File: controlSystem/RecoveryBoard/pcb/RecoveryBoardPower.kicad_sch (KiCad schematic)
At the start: 65 parts, among them J1 Conn_01x06, J10 Conn_01x02, J2 Thermistor, J3 Conn_01x04, J8 Conn_01x06, Q1 SI7465DP-T1-E3, U2 MP26123DR-LF-Z, U3 TPS63070

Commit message: Added rocket ready connector to ERS board
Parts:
- C10: value 100n -> 2.2n
- D4: value 1N4007 -> SS210A
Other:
- note removed: "ADD FLIGHT READY OR SIMiLAR PLUG"
- note removed: "ADD SEPARATE CONNECTOR FOR UMB INPUT ON INTERFACE BOARD?"
- note removed: "Check compv values"
- note removed: "Check values"
- note removed: "Swap for SS210A?"
- note removed: "Todo: Fix land pattern for footprint"
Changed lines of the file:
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@@
-    (effects (font (size 2.032 2.032)) (justify left bottom))
-  )
-  (text "ADD SEPARATE CONNECTOR FOR UMB INPUT ON INTERFACE BOARD?"
-    (at 73.66 134.62 0)
     (effects (font (size 2.032 2.032)) (justify left bottom))
   )
@@
     (effects (font (size 2.54 2.54)) (justify left bottom))
   )
-  (text "Swap for SS210A?" (at 220.98 129.54 0)
-    (effects (font (size 3.048 3.048)) (justify left bottom))
-  )
   (text "3S1P LiPo Battery" (at 281.94 132.08 0)
     (effects (font (size 1.27 1.27)) (justify left bottom))
@@
   )
   (text "Normally on\nShort ARM-IN with ARM-OUT to turn off" (at 266.7 48.26 0)
-    (effects (font (size 1.27 1.27)) (justify left bottom))
-  )
-  (text "Check compv values" (at 223.52 172.72 0)
     (effects (font (size 1.27 1.27)) (justify left bottom))
   )
@@
     (at 78.74 83.82 0)
     (effects (font (size 1.27 1.27)) (justify left bottom))
-  )
-  (text "Todo: Fix land pattern for footprint" (at 209.55 239.395 0)
-    (effects (font (size 1.27 1.27)) (justify left bottom))
-  )
-  (text "Check values" (at 220.98 228.6 0)
-    (effects (font (size 1.27 1.27)) (justify left bottom))
-  )
-  (text "ADD FLIGHT READY OR SIMiLAR PLUG" (at 73.66 139.7 0)
-    (effects (font (size 2.032 2.032)) (justify left bottom))
   )
   (text "LiPo Battery Charger" (at 208.28 101.6 0)
@@
       (effects (font (size 1.27 1.27)) (justify left))
     )
-    (property "Value" "100n" (id 1) (at 228.6 158.7562 0)
+    (property "Value" "2.2n" (id 1) (at 228.6 158.7562 0)
       (effects (font (size 1.27 1.27)) (justify left))
     )
@@
       (effects (font (size 1.27 1.27)) (justify left))
     )
-    (property "Value" "1N4007" (id 1) (at 228.6 125.4759 90)
-      (effects (font (size 1.27 1.27)) (justify left))
-    )
+    (property "Value" "SS210A" (id 1) (at 228.6 125.4759 90)
+      (effects (font (size 1.27 1.27)) (justify left))
+    )

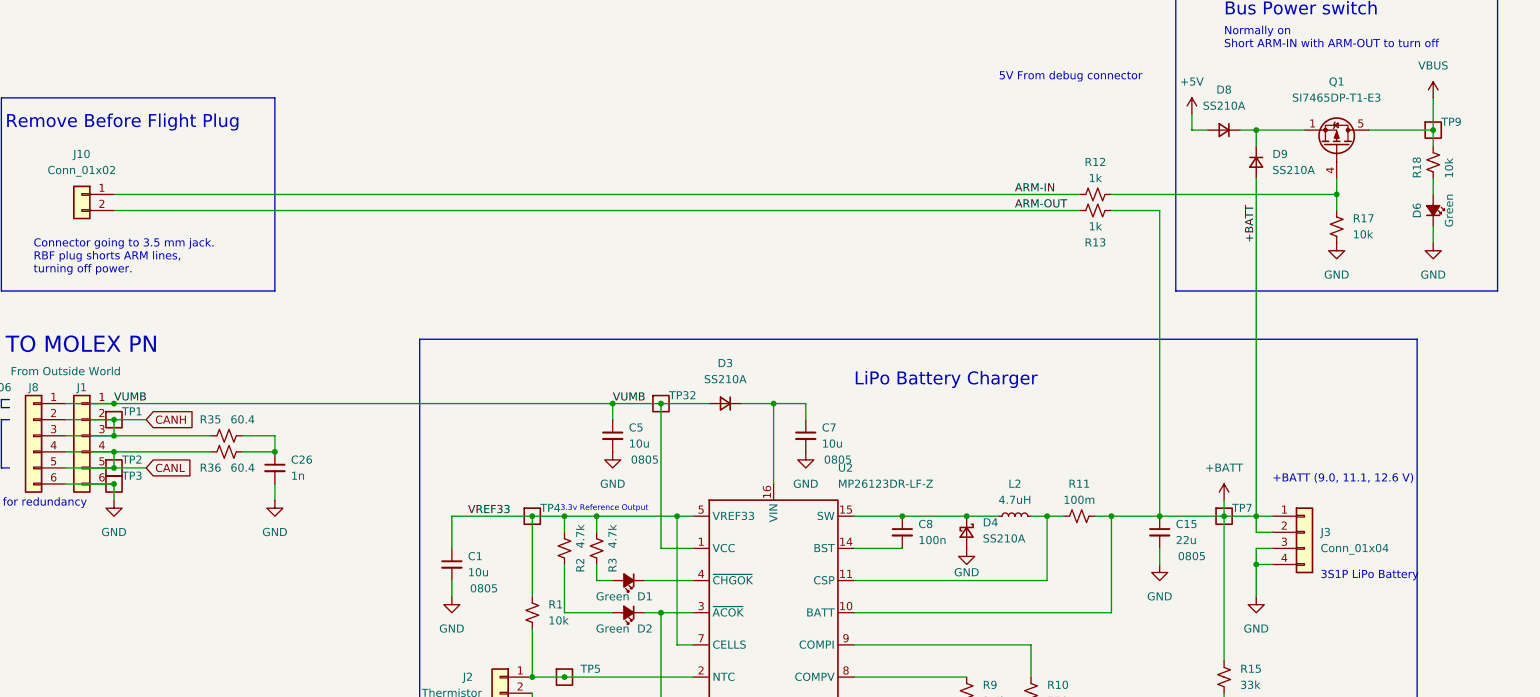
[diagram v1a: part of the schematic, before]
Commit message: Design review changes and cleaned up board layout.
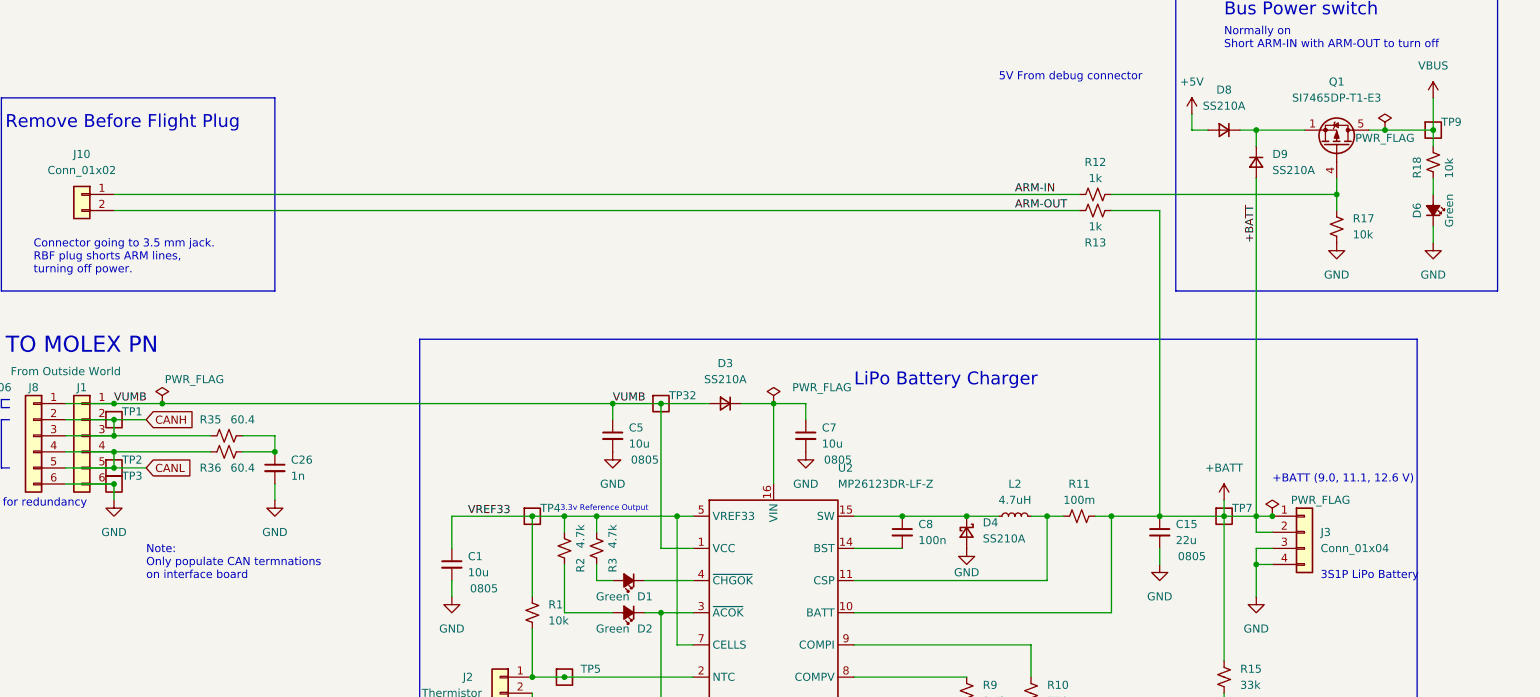
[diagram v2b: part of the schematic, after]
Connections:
- net +3.3V: now also U3.TIE2 (VOUT)
- net VBUS: now also U3.TIE1 (VIN)
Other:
- note added: "Note: Only populate CAN termnations on interface board"
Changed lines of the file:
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@@
   (junction (at 256.54 121.92) (diameter 0) (color 0 0 0 0)
   )
+  (junction (at 292.1 60.96) (diameter 0) (color 0 0 0 0)
+  )
   (junction (at 299.72 60.96) (diameter 0) (color 0 0 0 0)
   )
@@
   (junction (at 91.44 111.76) (diameter 0) (color 0 0 0 0)
   )
+  (junction (at 99.06 104.14) (diameter 0) (color 0 0 0 0)
+  )
   (junction (at 167.64 121.92) (diameter 0) (color 0 0 0 0)
   )
@@
   )
   (junction (at 271.78 60.96) (diameter 0) (color 0 0 0 0)
+  )
+  (junction (at 274.32 121.92) (diameter 0) (color 0 0 0 0)
   )
   (junction (at 91.44 114.3) (diameter 0) (color 0 0 0 0)
@@
     (stroke (width 0) (type default) (color 0 0 0 0))
   )
-  (wire (pts (xy 289.56 60.96) (xy 299.72 60.96))
+  (wire (pts (xy 289.56 60.96) (xy 292.1 60.96))
     (stroke (width 0) (type default) (color 0 0 0 0))
   )
@@
     (stroke (width 0) (type default) (color 0 0 0 0))
   )
+  (wire (pts (xy 292.1 60.96) (xy 299.72 60.96))
+    (stroke (width 0) (type default) (color 0 0 0 0))
+  )
   (wire (pts (xy 274.32 127) (xy 271.78 127))
     (stroke (width 0) (type default) (color 0 0 0 0))
@@
     (stroke (width 0) (type default) (color 0 0 0 0))
   )
+  (wire (pts (xy 99.06 104.14) (xy 170.18 104.14))
+    (stroke (width 0) (type default) (color 0 0 0 0))
+  )
   (wire (pts (xy 271.78 129.54) (xy 271.78 134.62))
     (stroke (width 0) (type default) (color 0 0 0 0))
@@
     (stroke (width 0) (type solid) (color 0 0 0 0))
   )
-  (wire (pts (xy 91.44 104.14) (xy 170.18 104.14))
+  (wire (pts (xy 91.44 104.14) (xy 99.06 104.14))
     (stroke (width 0) (type default) (color 0 0 0 0))
   )
@@
   (text "3.3V Switching Regulator" (at 180.34 190.5 0)
     (effects (font (size 2.032 2.032)) (justify left bottom))
+  )
+  (text "Note:\nOnly populate CAN termnations\non interface board"
+    (at 96.52 132.08 0)
+    (effects (font (size 1.27 1.27)) (justify left bottom))
   )
   (text "19V Umbilical Power" (at 52.07 105.41 0)
@@
     (pin "2")
   )
+  (symbol (lib_id "power:PWR_FLAG") (at 292.1 60.96 0) (unit 1)
+    (in_bom yes) (on_board yes)
+    (property "Reference" "#FLG0104" (id 0) (at 292.1 59.055 0)
+      (effects (font (size 1.27 1.27)) hide)
+    )
+    (property "Value" "PWR_FLAG" (id 1) (at 292.1 62.23 0))
+    (property "Footprint" "" (id 2) (at 292.1 60.96 0)
+      (effects (font (size 1.27 1.27)) hide)
+    )
+    (property "Datasheet" "~" (id 3) (at 292.1 60.96 0)
+      (effects (font (size 1.27 1.27)) hide)
+    )
+    (pin "1")
+  )
+  (symbol (lib_id "power:PWR_FLAG") (at 274.32 121.92 0) (unit 1)
+    (in_bom yes) (on_board yes)
+    (property "Reference" "#FLG0102" (id 0) (at 274.32 120.015 0)
+      (effects (font (size 1.27 1.27)) hide)
+    )
+    (property "Value" "PWR_FLAG" (id 1) (at 281.94 119.38 0))
+    (property "Footprint" "" (id 2) (at 274.32 121.92 0)
+      (effects (font (size 1.27 1.27)) hide)
+    )
+    (property "Datasheet" "~" (id 3) (at 274.32 121.92 0)
+      (effects (font (size 1.27 1.27)) hide)
+    )
+    (pin "1")
+  )
   (symbol (lib_id "power:GND") (at 248.92 220.98 0) (unit 1)
     (in_bom yes) (on_board yes) (fields_autoplaced)
@@
     (pin "1")
     (pin "2")
+  )
+  (symbol (lib_id "power:PWR_FLAG") (at 195.58 104.14 0) (unit 1)
+    (in_bom yes) (on_board yes)
+    (property "Reference" "#FLG0105" (id 0) (at 195.58 102.235 0)
+      (effects (font (size 1.27 1.27)) hide)
+    )
+    (property "Value" "PWR_FLAG" (id 1) (at 203.2 101.6 0))
+    (property "Footprint" "" (id 2) (at 195.58 104.14 0)
+      (effects (font (size 1.27 1.27)) hide)
+    )
+    (property "Datasheet" "~" (id 3) (at 195.58 104.14 0)
+      (effects (font (size 1.27 1.27)) hide)
+    )
+    (pin "1")
   )
   (symbol (lib_id "Device:R_Small_US") (at 266.7 157.48 0) (unit 1)
@@
     (pin "8")
     (pin "9")
+    (pin "TIE1")
+    (pin "TIE2")
   )
   (symbol (lib_id "power:GND") (at 167.64 220.98 0) (unit 1)
@@
       (effects (font (size 1.27 1.27)) hide)
     )
+    (pin "1")
+  )
+  (symbol (lib_id "power:PWR_FLAG") (at 99.06 104.14 0) (unit 1)
+    (in_bom yes) (on_board yes)
+    (property "Reference" "#FLG0101" (id 0) (at 99.06 102.235 0)
+      (effects (font (size 1.27 1.27)) hide)
+    )
+    (property "Value" "PWR_FLAG" (id 1) (at 104.14 100.33 0))
+    (property "Footprint" "" (id 2) (at 99.06 104.14 0)
+      (effects (font (size 1.27 1.27)) hide)
+    )
+    (property "Datasheet" "~" (id 3) (at 99.06 104.14 0)
+      (effects (font (size 1.27 1.27)) hide)
+    )

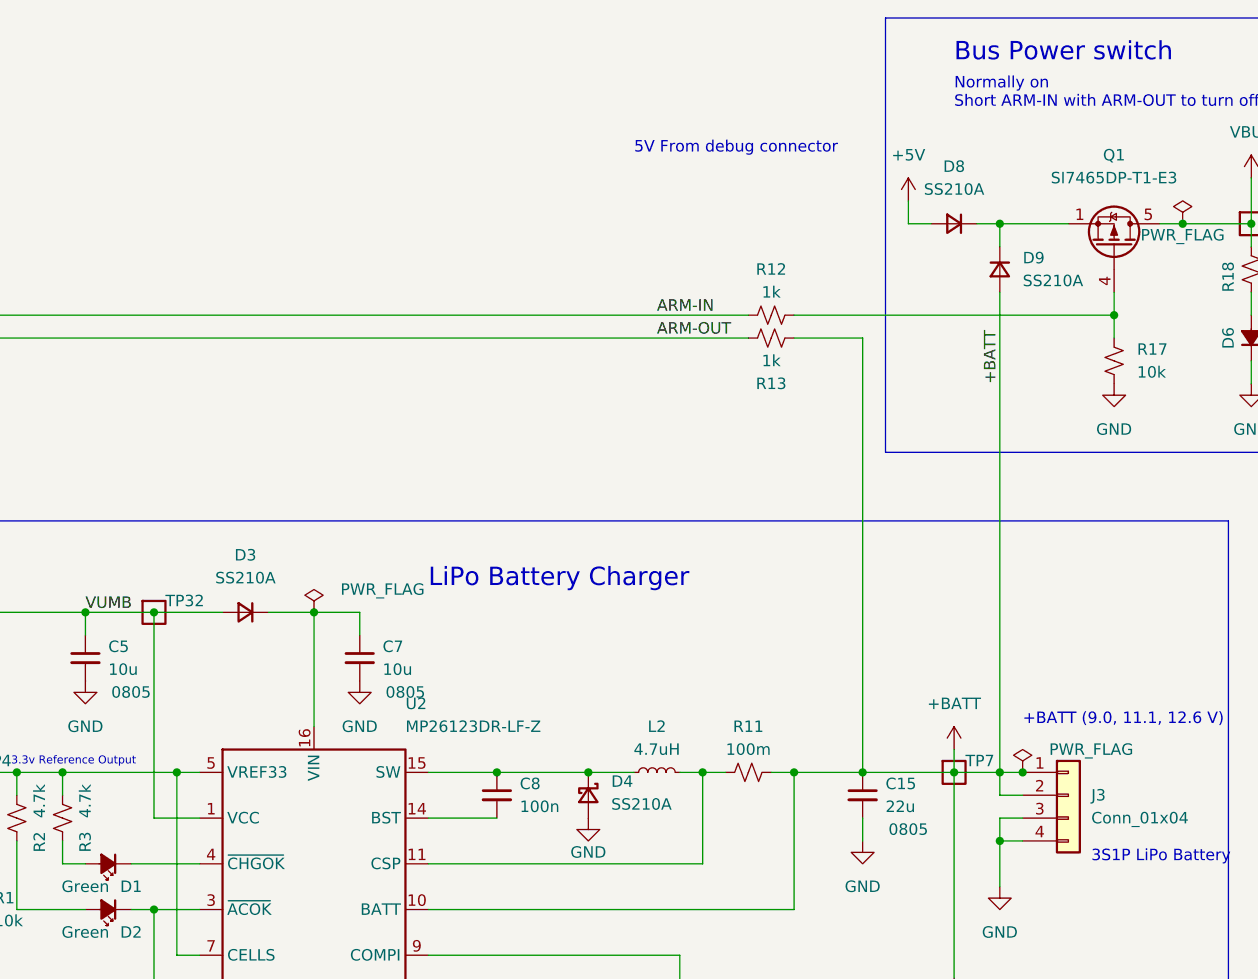
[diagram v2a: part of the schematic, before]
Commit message: Updated ERS board stencil cutout for Q1
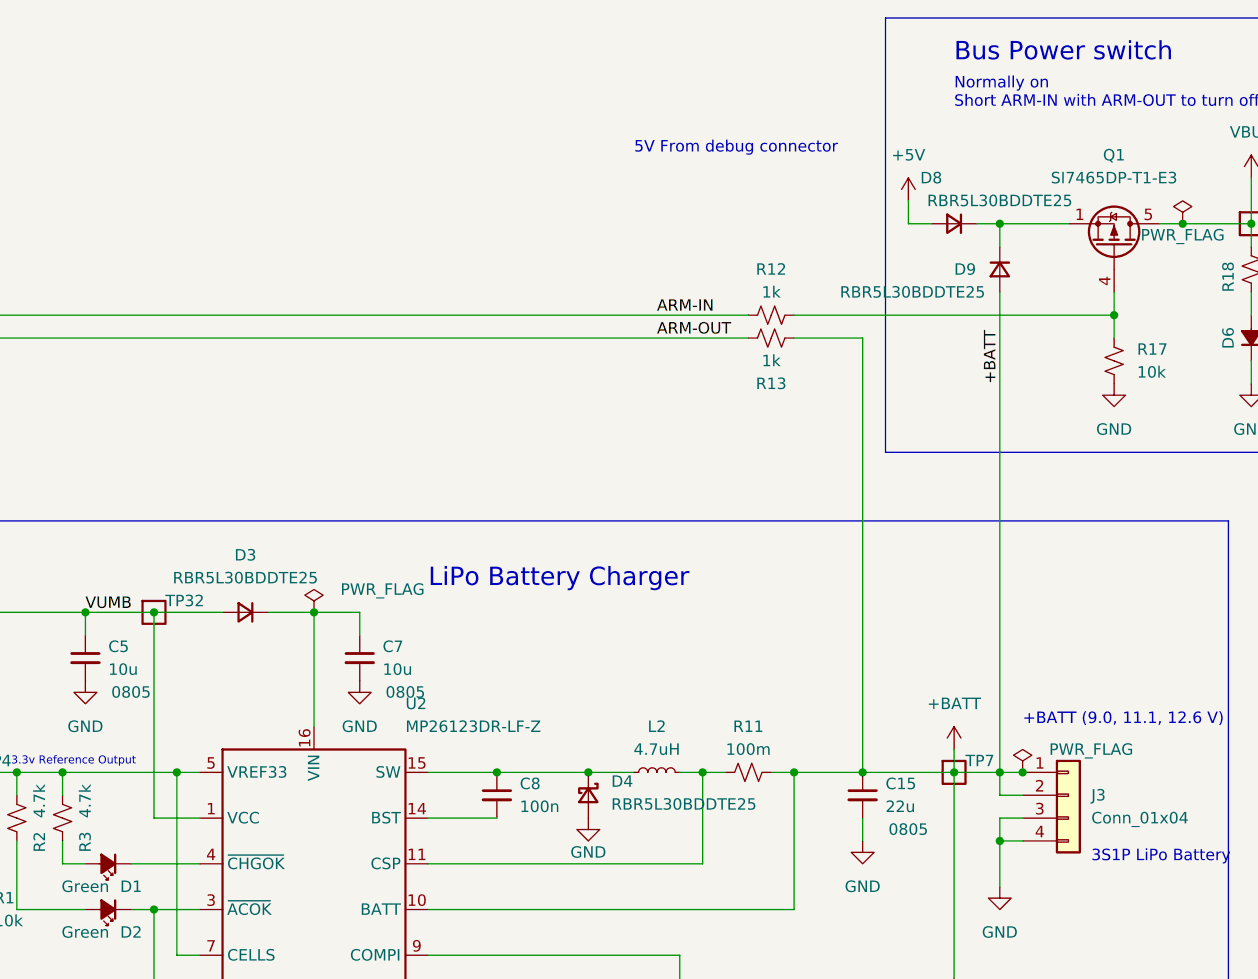
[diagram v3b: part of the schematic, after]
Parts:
- C15: MPN (none) -> GRT21BR61E226ME13L
- D3, D4, D8, D9: value SS210A -> RBR5L30BDDTE25
- Q1: footprint Package_SO:PowerPAK_SO-8_Single -> psas-footprints:PowerPAK_SO-8_Single
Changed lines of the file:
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@@
   )
   (symbol (lib_id "Device:D_Small") (at 266.7 60.96 180) (unit 1)
-    (in_bom yes) (on_board yes) (fields_autoplaced)
-    (property "Reference" "D8" (id 0) (at 266.7 54.61 0))
-    (property "Value" "SS210A" (id 1) (at 266.7 57.15 0))
+    (in_bom yes) (on_board yes)
+    (property "Reference" "D8" (id 0) (at 264.16 55.88 0))
+    (property "Value" "RBR5L30BDDTE25" (id 1) (at 271.78 58.42 0))
     (property "Footprint" "Diode_SMD:D_SMA" (id 2) (at 266.7 60.96 90)
       (effects (font (size 1.27 1.27)) hide)
@@
     )
     (property "Field4" "0805" (id 4) (at 261.62 128.27 0))
+    (property "MPN" "GRT21BR61E226ME13L" (id 5) (at 256.54 124.46 0)
+      (effects (font (size 1.27 1.27)) hide)
+    )
     (pin "1")
     (pin "2")
@@
     (property "Reference" "Q1" (id 0) (at 284.48 53.34 90))
     (property "Value" "SI7465DP-T1-E3" (id 1) (at 284.48 55.88 90))
-    (property "Footprint" "Package_SO:PowerPAK_SO-8_Single" (id 2) (at 282.575 58.42 0)
+    (property "Footprint" "psas-footprints:PowerPAK_SO-8_Single" (id 2) (at 282.575 58.42 0)
       (effects (font (size 1.27 1.27) italic) (justify left) hide)
     )
@@
     (in_bom yes) (on_board yes) (fields_autoplaced)
     (property "Reference" "D3" (id 0) (at 187.96 97.79 0))
-    (property "Value" "SS210A" (id 1) (at 187.96 100.33 0))
+    (property "Value" "RBR5L30BDDTE25" (id 1) (at 187.96 100.33 0))
     (property "Footprint" "Diode_SMD:D_SMA" (id 2) (at 187.96 104.14 90)
       (effects (font (size 1.27 1.27)) hide)
@@
   )
   (symbol (lib_id "Device:D_Small") (at 271.78 66.04 270) (unit 1)
-    (in_bom yes) (on_board yes) (fields_autoplaced)
-    (property "Reference" "D9" (id 0) (at 274.32 64.7699 90)
-      (effects (font (size 1.27 1.27)) (justify left))
-    )
-    (property "Value" "SS210A" (id 1) (at 274.32 67.3099 90)
+    (in_bom yes) (on_board yes)
+    (property "Reference" "D9" (id 0) (at 266.7 66.04 90)
+      (effects (font (size 1.27 1.27)) (justify left))
+    )
+    (property "Value" "RBR5L30BDDTE25" (id 1) (at 254 68.58 90)
       (effects (font (size 1.27 1.27)) (justify left))
     )
@@
       (effects (font (size 1.27 1.27)) (justify left))
     )
-    (property "Value" "SS210A" (id 1) (at 228.6 125.4759 90)
-      (effects (font (size 1.27 1.27)) (justify left))
-    )
+    (property "Value" "RBR5L30BDDTE25" (id 1) (at 228.6 125.4759 90)
+      (effects (font (size 1.27 1.27)) (justify left))
+    )
